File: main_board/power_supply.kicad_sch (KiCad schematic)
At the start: 41 parts, among them Q2 Q_FDC6561AN, SW9 1825232-1, U1 INA219BIDR, U2 MIC2250-1YD5-TR, U3 MCP73871T-2CCI/ML, U5 AP9101CAK6-ABTRG1

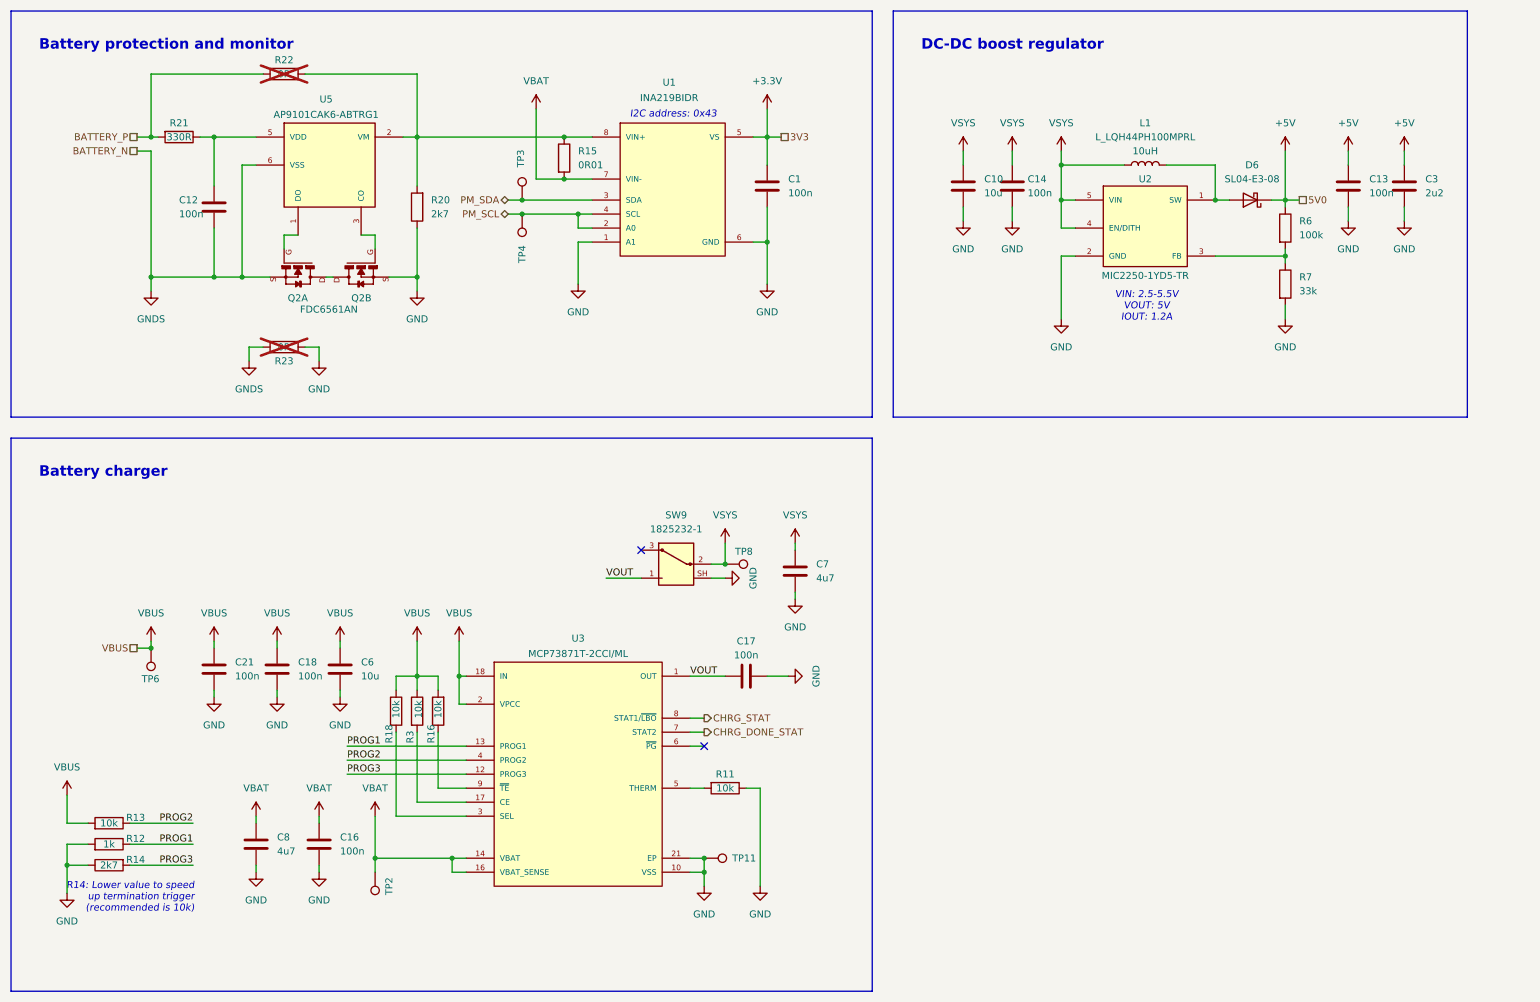
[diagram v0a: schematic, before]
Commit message: Add TODOs from rev.1.1 bringup
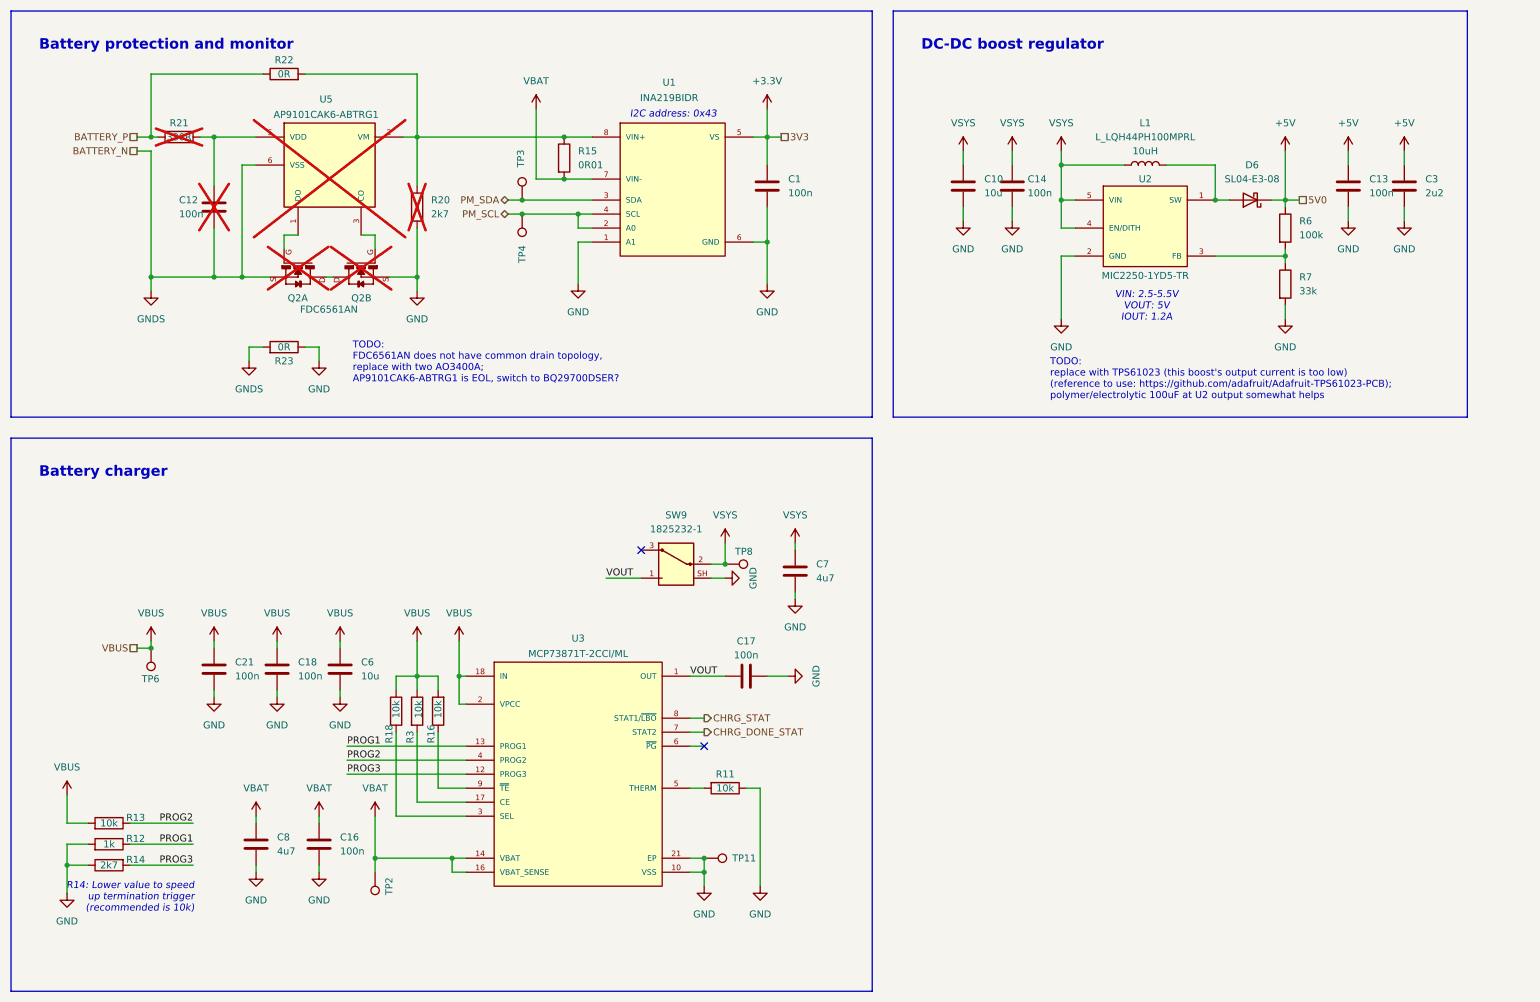
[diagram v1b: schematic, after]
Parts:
- C12, Q2, R20, R21, U5: now not fitted
- R22, R23: now fitted
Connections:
- net GND: now also R23.1; no longer R23.2
- net GNDS: now also R23.2; no longer R23.1
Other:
- note added: "TODO: FDC6561AN does not have common drain topology, replace with two AO3400A; AP9101CAK6-ABTRG1 is EOL, switch to BQ29700DSER?"
- note added: "TODO: replace with TPS61023 (this boost's output current is too low) (reference to use: https://github.com/adafruit/Adafruit-TPS61023-PCB); polymer/electrolytic 100uF at U2 output somewhat helps"

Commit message: Update README's troubleshooting section, update bringup TODOs
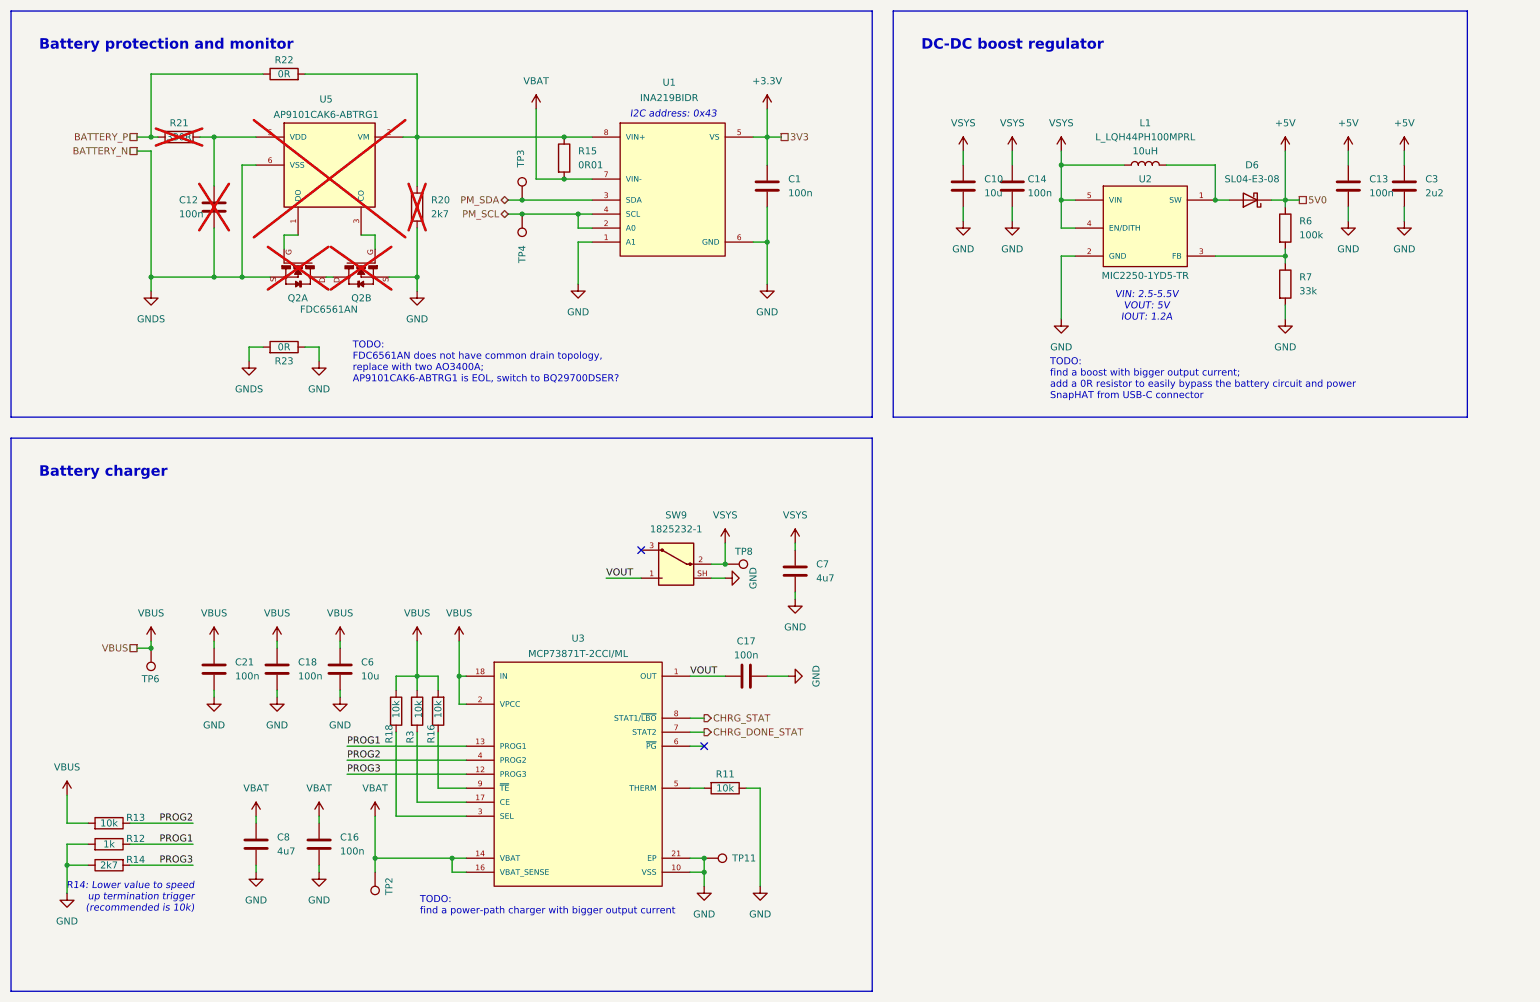
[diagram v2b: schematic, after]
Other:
- note added: "TODO: find a boost with bigger output current; add a 0R resistor to easily bypass the battery circuit and power SnapHAT from USB-C connector"
- note added: "TODO: find a power-path charger with bigger output current"
- note removed: "TODO: replace with TPS61023 (this boost's output current is too low) (reference to use: https://github.com/adafruit/Adafruit-TPS61023-PCB); polymer/electrolytic 100uF at U2 output somewhat helps"
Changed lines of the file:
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@@
 		)
 	)
-	(text "TODO:\nreplace with TPS61023 (this boost's output current is too low)\n(reference to use: https://github.com/adafruit/Adafruit-TPS61023-PCB);\npolymer/electrolytic 100uF at U2 output somewhat helps "
+	(text "TODO:\nfind a power-path charger with bigger output current"
+		(exclude_from_sim no)
+		(at 90.678 178.816 0)
+		(effects
+			(font
+				(face "Quicksand")
+				(size 1.27 1.27)
+			)
+			(justify left)
+		)
+	)
+	(text "TODO:\nfind a boost with bigger output current;\nadd a 0R resistor to easily bypass the battery circuit and power \nSnapHAT from USB-C connector"
 		(exclude_from_sim no)
 		(at 204.978 83.312 0)
